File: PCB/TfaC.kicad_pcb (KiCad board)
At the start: 2 copper layers, 0 parts

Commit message: Added the switch footprints and started the layout
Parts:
- added ALMint1: ALMint, Pin_Headers:Pin_Header_Straight_1x01, F.Cu at (108.5, 116.3)
- added C201: 1u, Capacitors_SMD:C_0805_HandSoldering, F.Cu at (133.2, 98.9)
- added C202: 1u, Capacitors_SMD:C_0805_HandSoldering, F.Cu at (182.6, 78.1)
- added C203: 1u, Capacitors_SMD:C_0805_HandSoldering, F.Cu at (177.7, 82.8)
- added C204: 1u, Capacitors_SMD:C_0805_HandSoldering, F.Cu at (129.7, 94.8)
- added C501: 100n, Capacitors_SMD:C_0805_HandSoldering, F.Cu at (150.1, 95.1)
- added DCFint1: DCFint, Pin_Headers:Pin_Header_Straight_1x01, F.Cu at (112.0, 116.3)
- added IC501: ATMEGA88-A, Housings_QFP:LQFP-32_7x7mm_Pitch0.8mm, F.Cu at (147.3, 88.8)
- added M301: DisplayModule, Pin_Headers:Pin_Header_Angled_1x05, F.Cu at (167.0, 114.0)
- added P101: Line, Pin_Headers:Pin_Header_Straight_1x02, F.Cu at (193.2, 67.9)
- added P201: GND, Pin_Headers:Pin_Header_Straight_1x01, F.Cu at (183.5, 68.1)
- added P202: Vin, Pin_Headers:Pin_Header_Straight_1x01, F.Cu at (180.0, 68.1)
- added P203: Vcc, Pin_Headers:Pin_Header_Straight_1x01, F.Cu at (193.7, 73.9)
- added P204: Vbb, Pin_Headers:Pin_Header_Straight_1x01, F.Cu at (199.0, 86.2)
- added P501: PRG, Pin_Headers:Pin_Header_Straight_2x03, F.Cu at (139.8, 75.4)
- added Q401: IRLML2502, tfac-footprints:Micro3, F.Cu at (121.7, 104.1)
- added Q402: IRLML2502, tfac-footprints:Micro3, F.Cu at (114.2, 104.1)
- added Q403: IRLML2502, tfac-footprints:Micro3, F.Cu at (124.1, 87.9)
- added Q404: IRLML2502, tfac-footprints:Micro3, F.Cu at (109.3, 87.9)
- added Q405: IRLML2502, tfac-footprints:Micro3, F.Cu at (101.9, 87.9)
- added Q406: IRLML2502, tfac-footprints:Micro3, F.Cu at (116.7, 87.9)
- added Q407: NOPOP, tfac-footprints:Micro3, F.Cu at (106.8, 104.1)
- added Q408: IRLML2502, tfac-footprints:Micro3, F.Cu at (99.3, 104.3)
- added R201: 0, Resistors_SMD:R_0805_HandSoldering, F.Cu at (135.6, 99.0)
- added R401: 10K, Resistors_SMD:R_0805_HandSoldering, F.Cu at (124.7, 104.9)
- added R402: 1K5, Resistors_SMD:R_0805_HandSoldering, F.Cu at (122.4, 101.2)
- added R403: 10K, Resistors_SMD:R_0805_HandSoldering, F.Cu at (117.2, 104.9)
- added R404: 1K5, Resistors_SMD:R_0805_HandSoldering, F.Cu at (114.9, 101.2)
- added R405: 10K, Resistors_SMD:R_0805_HandSoldering, F.Cu at (121.2, 87.1)
- added R406: 4K7, Resistors_SMD:R_0805_HandSoldering, F.Cu at (123.3, 90.8)
- added R407: 10K, Resistors_SMD:R_0805_HandSoldering, F.Cu at (106.4, 87.1)
- added R408: 4K7, Resistors_SMD:R_0805_HandSoldering, F.Cu at (108.6, 90.8)
- added R409: 10K, Resistors_SMD:R_0805_HandSoldering, F.Cu at (98.8, 87.1)
- added R410: 4K7, Resistors_SMD:R_0805_HandSoldering, F.Cu at (101.1, 90.8)
- added R411: 10K, Resistors_SMD:R_0805_HandSoldering, F.Cu at (113.8, 87.1)
- added R412: 4K7, Resistors_SMD:R_0805_HandSoldering, F.Cu at (116.0, 90.8)
- added R413: NOPOP, Resistors_SMD:R_0805_HandSoldering, F.Cu at (109.9, 105.0)
- added R414: NOPOP, Resistors_SMD:R_0805_HandSoldering, F.Cu at (107.6, 101.2)
- added R415: 10K, Resistors_SMD:R_0805_HandSoldering, F.Cu at (102.4, 105.0)
- added R416: 4K7, Resistors_SMD:R_0805_HandSoldering, F.Cu at (100.1, 101.3)
- added R501: 10K, Resistors_SMD:R_0805_HandSoldering, F.Cu at (150.2, 97.4)
- added SW501: Time Set, tfac-footprints:TL3315, B.Cu at (171.5, 80.5)
- added SW502: Alarm Set, tfac-footprints:TL3315, B.Cu at (186.0, 80.5)
- added SW503: Fast, tfac-footprints:TL3315, B.Cu at (171.5, 95.5)
- added SW504: Slow, tfac-footprints:TL3315, B.Cu at (186.0, 95.5)
- added SW505: Auto Time, tfac-footprints:AYZ0202AGRLC, B.Cu at (161.5, 74.0)
- added SW506: Sleep, tfac-footprints:TL3315, F.Cu at (198.0, 115.5)
- added SW507: Summer Time, Pin_Headers:Pin_Header_Straight_1x02, F.Cu at (169.8, 68.3)
- added SW508: Alarm Enabled, tfac-footprints:CLSB12C01, F.Cu at (161.2, 86.2)
- added TP-MISO1: MISO, Pin_Headers:Pin_Header_Straight_1x01, F.Cu at (105.4, 75.4)
- added TP-MOSI1: MOSI, Pin_Headers:Pin_Header_Straight_1x01, F.Cu at (109.2, 75.4)
- added TP-Pint1: Pint, Pin_Headers:Pin_Header_Straight_1x01, F.Cu at (115.6, 116.3)
- added TP-SCK1: SCK, Pin_Headers:Pin_Header_Straight_1x01, F.Cu at (113.0, 75.6)
- added TP-SS1: SS1, Pin_Headers:Pin_Header_Straight_1x01, F.Cu at (156.5, 109.3)
- added TP-SS2: SS2, Pin_Headers:Pin_Header_Straight_1x01, F.Cu at (116.7, 75.6)
- added U201: MCP1703T-5002E/CB, tfac-footprints:SOT-23A, F.Cu at (199.0, 72.4)
- added U202: LD2979, tfac-footprints:SOT-23-5L, F.Cu at (129.6, 97.7)
- added U401: RTC-DCF77, tfac-footprints:RTC-DCF, F.Cu at (111.8, 96.2)
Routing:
- net L_MISO: track 0.00 -> 15.3 mm
- net ~L_SS: track 0.00 -> 11.9 mm
- net L_MOSI: track 0.00 -> 9.52 mm
- net L_SCK: track 0.00 -> 8.09 mm
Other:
- net class Default: clearance 0.2 -> 0.254; trace_width 0.25 -> 0.254; via_dia 0.6 -> 0.6858; via_drill 0.4 -> 0.3302
- rule trace_clearance: 0.2 -> 0.254
- rule trace_min: 0.2 -> 0.1524
- rule via_min_drill: 0.3 -> 0.3302
- rule via_min_size: 0.4 -> 0.6858

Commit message: Started the layout
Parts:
- removed ALMint1: ALMint, Pin_Headers:Pin_Header_Straight_1x01
- removed DCFint1: DCFint, Pin_Headers:Pin_Header_Straight_1x01
- removed P201: GND, Pin_Headers:Pin_Header_Straight_1x01
- removed P202: Vin, Pin_Headers:Pin_Header_Straight_1x01
- removed P203: Vcc, Pin_Headers:Pin_Header_Straight_1x01
- removed P204: Vbb, Pin_Headers:Pin_Header_Straight_1x01
- removed TP-MISO1: MISO, Pin_Headers:Pin_Header_Straight_1x01
- removed TP-MOSI1: MOSI, Pin_Headers:Pin_Header_Straight_1x01
- removed TP-Pint1: Pint, Pin_Headers:Pin_Header_Straight_1x01
- removed TP-SCK1: SCK, Pin_Headers:Pin_Header_Straight_1x01
- added REF**: MountingHole_2-7mm, Mounting_Holes:MountingHole_2-7mm, F.Cu at (103.0, 76.0)
- added REF**: MountingHole_2-7mm, Mounting_Holes:MountingHole_2-7mm, F.Cu at (142.0, 76.0)
- added REF**: MountingHole_2-7mm, Mounting_Holes:MountingHole_2-7mm, F.Cu at (103.0, 86.0)
- added REF**: MountingHole_2-7mm, Mounting_Holes:MountingHole_2-7mm, F.Cu at (142.0, 86.0)
- added TP1: CONN_01X06, Pin_Headers:Pin_Header_Straight_1x06, F.Cu at (102.1, 96.3)
- added TP2: CONN_01X06, Pin_Headers:Pin_Header_Straight_1x06, F.Cu at (143.0, 96.3)
- M301: footprint Pin_Headers:Pin_Header_Angled_1x05 -> Pin_Headers:Pin_Header_Straight_1x05
- SW506: moved to B.Cu
- moved C201 62.1 mm to (189.0, 71.6)
- moved C204 59.3 mm to (182.6, 68.1)
- moved U202 59.2 mm to (182.6, 71.4)
- moved R201 57.8 mm to (186.4, 71.6)
- moved R416 56.4 mm to (155.7, 110.7), turned to 270 degrees
- moved Q408 52.2 mm to (151.1, 110.7), turned to 270 degrees
- moved P501 48.8 mm to (178.3, 105.4), turned to 90 degrees
- moved R414 48.0 mm to (155.4, 104.1), turned to 270 degrees
- moved R415 45.6 mm to (147.6, 110.7)
- moved Q407 44.3 mm to (151.1, 104.1), turned to 270 degrees
- moved R404 40.6 mm to (155.4, 98.0), turned to 270 degrees
- moved C501 38.7 mm to (188.0, 87.1), turned to 90 degrees
- moved R413 37.7 mm to (147.6, 104.4)
- moved Q402 37.2 mm to (150.9, 98.0), turned to 270 degrees
- moved R501 36.7 mm to (185.4, 87.1), turned to 270 degrees
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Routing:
- net /Controller/SCK: track 0.19 -> 126.4 mm, vias 0 -> 2
- net /Controller/MISO: track 0.19 -> 111.3 mm
- net /Power System/Vbb: track 0.00 -> 96.5 mm, vias 0 -> 7
- net GND: track 0.00 -> 73.4 mm, vias 0 -> 6
- net /Controller/~DISPLAY_SELECT: track 0.00 -> 52.9 mm, vias 0 -> 1
- net /Controller/MOSI: track 0.19 -> 34.7 mm
- net /Power System/Vin: track 0.00 -> 24.0 mm
- net Fast: track 0.00 -> 18.3 mm, vias 0 -> 1
- net Alarm_Enabled: track 0.00 -> 16.8 mm
- net L_ALARM_INT: track 0.00 -> 16.7 mm
- net L_Periodic_INT: track 0.00 -> 16.5 mm
- net Reset: track 0.00 -> 16.5 mm, vias 0 -> 4
- net L_Rx: track 0.00 -> 13.9 mm
- net Slow: track 0.00 -> 13.8 mm, vias 0 -> 1
- net L_DCF_RCPT: track 0.00 -> 13.3 mm
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- added copper zone on B.Cu, net /Power System/Vbb
- added copper zone on F.Cu, net GND
- added copper zone on B.Cu, net Reset

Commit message: Trying out an alternative layout
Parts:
- moved P101 50.3 mm to (147.6, 68.1)
- moved C202 48.0 mm to (149.6, 79.5), turned to 270 degrees
- moved U201 44.3 mm to (153.2, 79.5), turned to 270 degrees
- moved R201 42.6 mm to (146.3, 85.9)
- moved REF** 42.5 mm to (99.5, 74.8), turned to 90 degrees
- moved C204 41.4 mm to (148.6, 91.7), turned to 180 degrees
- moved C203 40.2 mm to (153.2, 82.3), turned to 180 degrees
- moved C201 40.0 mm to (151.6, 85.9), turned to 270 degrees
- moved U202 37.6 mm to (149.1, 88.4), turned to 270 degrees
- moved REF** 36.6 mm to (99.5, 112.5), turned to 90 degrees
- moved REF** 34.4 mm to (109.5, 74.8), turned to 90 degrees
- moved R409 32.8 mm to (123.4, 83.4), turned to 90 degrees
- moved R416 31.9 mm to (140.0, 83.1)
- moved Q405 31.1 mm to (120.0, 83.2), turned to 90 degrees
- moved Q408 31.0 mm to (136.7, 83.3)
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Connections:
- C203 pad 1: Reset -> /Controller/Vcc
- C501 pad 1: Reset -> /Controller/Vcc
- IC501 pad 12: (no net) -> Net-(IC501-Pad12)
- IC501 pad 18: Net-(IC501-Pad18) -> /Controller/Vcc
- IC501 pad 19: (no net) -> Net-(IC501-Pad19)
- IC501 pad 20: (no net) -> Net-(IC501-Pad20)
- IC501 pad 22: (no net) -> Net-(IC501-Pad22)
- IC501 pad 26: (no net) -> Net-(IC501-Pad26)
- IC501 pad 27: (no net) -> Net-(IC501-Pad27)
- IC501 pad 28: (no net) -> Net-(IC501-Pad28)
- IC501 pad 4: Net-(IC501-Pad18) -> /Controller/Vcc
- IC501 pad 6: Net-(IC501-Pad18) -> /Controller/Vcc
- IC501 pad 7: (no net) -> Net-(IC501-Pad7)
- IC501 pad 8: (no net) -> Net-(IC501-Pad8)
- M301 pad 1: Reset -> /Controller/Vcc
- M301 pad 3: /Controller/MOSI -> /Controller/SCK
- M301 pad 4: /Controller/SCK -> /Controller/~DISPLAY_SELECT
- M301 pad 5: /Controller/~DISPLAY_SELECT -> GND
- P501 pad 2: Reset -> /Controller/Vcc
- R402 pad 1: Reset -> /Controller/Vcc
- R404 pad 1: Reset -> /Controller/Vcc
- R406 pad 1: Reset -> /Controller/Vcc
- R408 pad 1: Reset -> /Controller/Vcc
- R410 pad 1: Reset -> /Controller/Vcc
- R412 pad 1: Reset -> /Controller/Vcc
- R414 pad 1: Reset -> /Controller/Vcc
- R416 pad 1: Reset -> /Controller/Vcc
- R501 pad 1: Net-(IC501-Pad18) -> /Controller/Vcc
- SW505 pad 1: (no net) -> Net-(SW505-Pad1)
- SW508 pad 1: (no net) -> Net-(SW508-Pad1)
- U201 pad 3: Reset -> /Controller/Vcc
- U202 pad 4: (no net) -> Net-(U202-Pad4)
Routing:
- net /Controller/SCK: track 126.4 -> 11.6 mm, vias 2 -> 0
- net /Controller/MISO: track 111.3 -> 11.5 mm
- net /Controller/Vcc: track 0.00 -> 57.4 mm, vias 0 -> 5
- net /Power System/Vbb: track 96.5 -> 43.6 mm, vias 7 -> 8
- net /Controller/~DISPLAY_SELECT: track 52.9 -> 8.05 mm, vias 1 -> 0
- net GND: track 73.4 -> 36.0 mm, vias 6 -> 7
- net /Controller/MOSI: track 34.7 -> 10.9 mm
- net L_MISO: track 15.3 -> 38.5 mm
- net L_Periodic_INT: track 16.5 -> 38.8 mm
- net L_MOSI: track 10.8 -> 30.4 mm
- net L_DCF_RCPT: track 13.3 -> 30.8 mm
- net L_SCK: track 8.87 -> 21.9 mm
- net /Power System/Vin: track 24.0 -> 11.7 mm, vias 0 -> 3
- net Reset: track 16.5 -> 4.39 mm, vias 4 -> 0
- net /Controller/~RTC_SELECT: track 9.87 -> 21.9 mm
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- added copper zone on B.Cu, net /Controller/Vcc
- added copper zone on B.Cu, net /Power System/Vin
- removed copper zone on B.Cu, net Reset
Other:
- net class Default: clearance 0.254 -> 0.1524; trace_width 0.254 -> 0.1524
- rule trace_clearance: 0.254 -> 0.1524

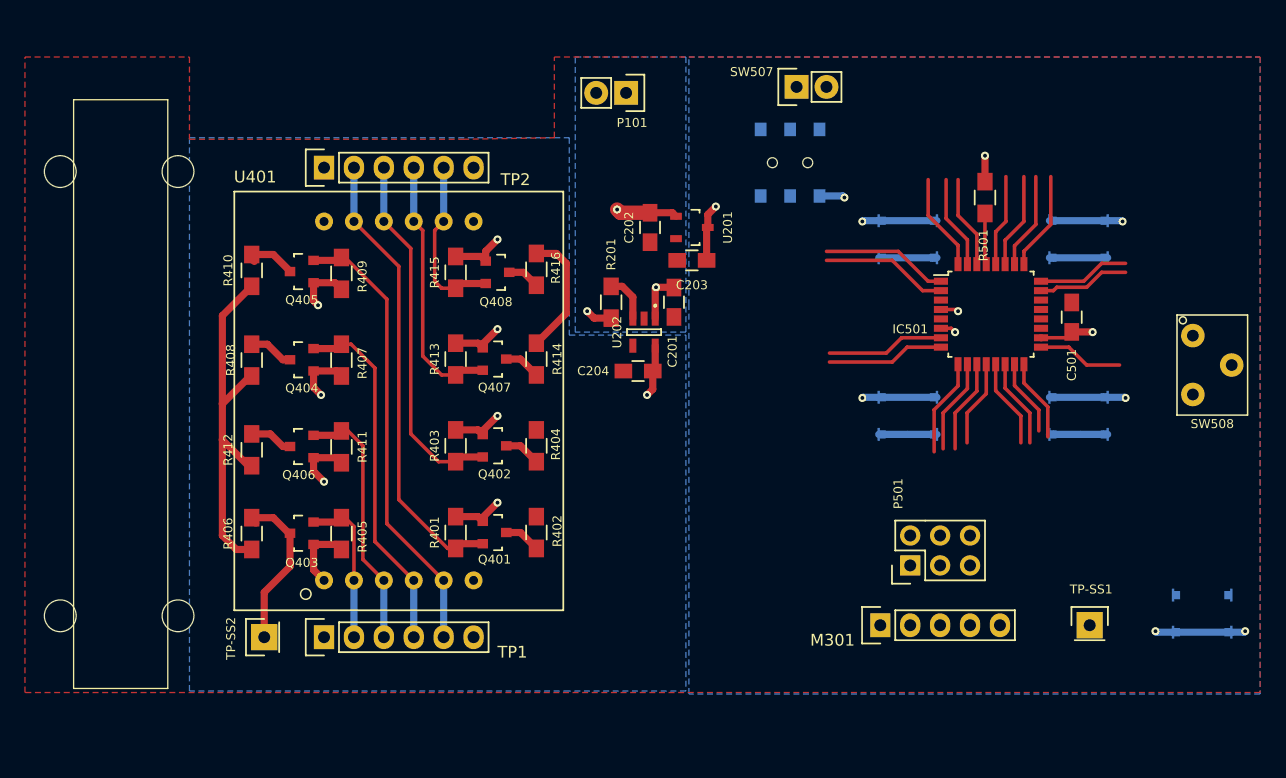
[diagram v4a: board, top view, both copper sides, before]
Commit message: Completed draft layout for the alternate layout
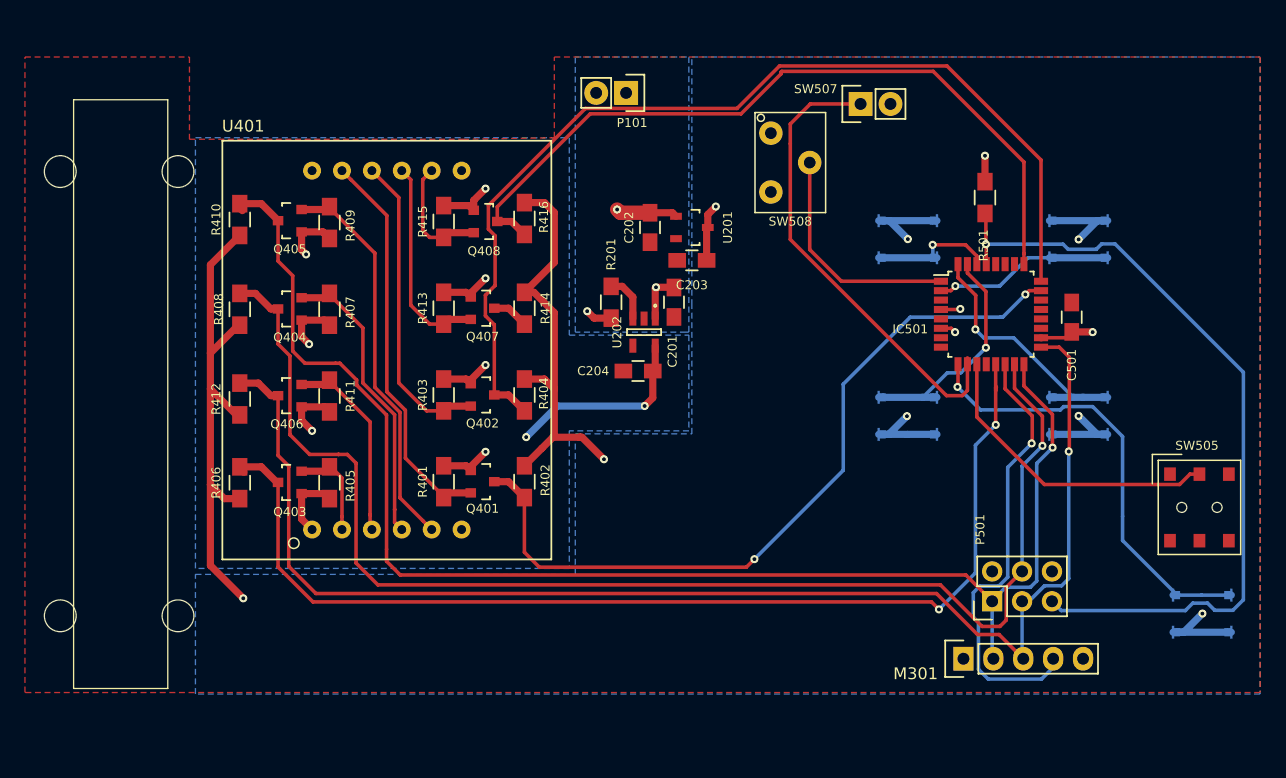
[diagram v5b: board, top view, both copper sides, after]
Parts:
- removed TP-SS1: SS1, Pin_Headers:Pin_Header_Straight_1x01
- removed TP-SS2: SS2, Pin_Headers:Pin_Header_Straight_1x01
- removed TP1, TP2: CONN_01X06, Pin_Headers:Pin_Header_Straight_1x06
- SW505: moved to F.Cu
- moved SW505 45.5 mm to (196.3, 103.3)
- moved SW508 39.8 mm to (161.5, 74.0)
- moved M301 7.61 mm to (176.2, 116.1)
- moved P501 7.60 mm to (178.7, 111.3)
- moved SW507 5.63 mm to (167.5, 69.0)
- moved R416 4.44 mm to (138.9, 78.7)
- moved Q406 4.44 mm to (119.0, 93.8)
- moved R402 4.44 mm to (138.9, 101.1)
- moved R404 4.44 mm to (138.9, 93.7)
- moved R414 4.44 mm to (138.9, 86.4)
- moved Q403 4.44 mm to (119.0, 101.2)
- moved R405 4.44 mm to (122.4, 101.2)
- moved R406 4.44 mm to (114.8, 101.2)
- moved R407 4.44 mm to (122.4, 86.4)
- moved R408 4.44 mm to (114.8, 86.4)
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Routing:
- net /Controller/MISO: track 11.5 -> 121.3 mm, vias 0 -> 1
- net /Controller/SCK: track 11.6 -> 116.1 mm, vias 0 -> 1
- net /Controller/MOSI: track 10.9 -> 112.4 mm, vias 0 -> 1
- net /Controller/DCF_RCPT: track 10.9 -> 85.5 mm
- net /Controller/~RTC_SELECT: track 21.9 -> 92.6 mm, vias 0 -> 2
- net Reset: track 4.39 -> 68.1 mm, vias 0 -> 1
- net /Controller/Periodic_INT: track 10.9 -> 66.2 mm, vias 0 -> 2
- net /Controller/ALARM_INT: track 11.1 -> 65.5 mm
- net /Controller/Vcc: track 57.4 -> 93.7 mm, vias 5 -> 7
- net Summer_Time: track 8.03 -> 40.0 mm
- net /Controller/~DISPLAY_SELECT: track 8.05 -> 38.5 mm, vias 0 -> 1
- net Sleep: track 8.27 -> 38.4 mm, vias 0 -> 1
- net Auto_Time: track 7.95 -> 26.1 mm
- net /Power System/Vbb: track 43.6 -> 56.1 mm, vias 8 -> 9
- net Net-(IC501-Pad7): track 10.0 -> 0.00 mm
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
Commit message: Completed the layout and generated the Gerbers
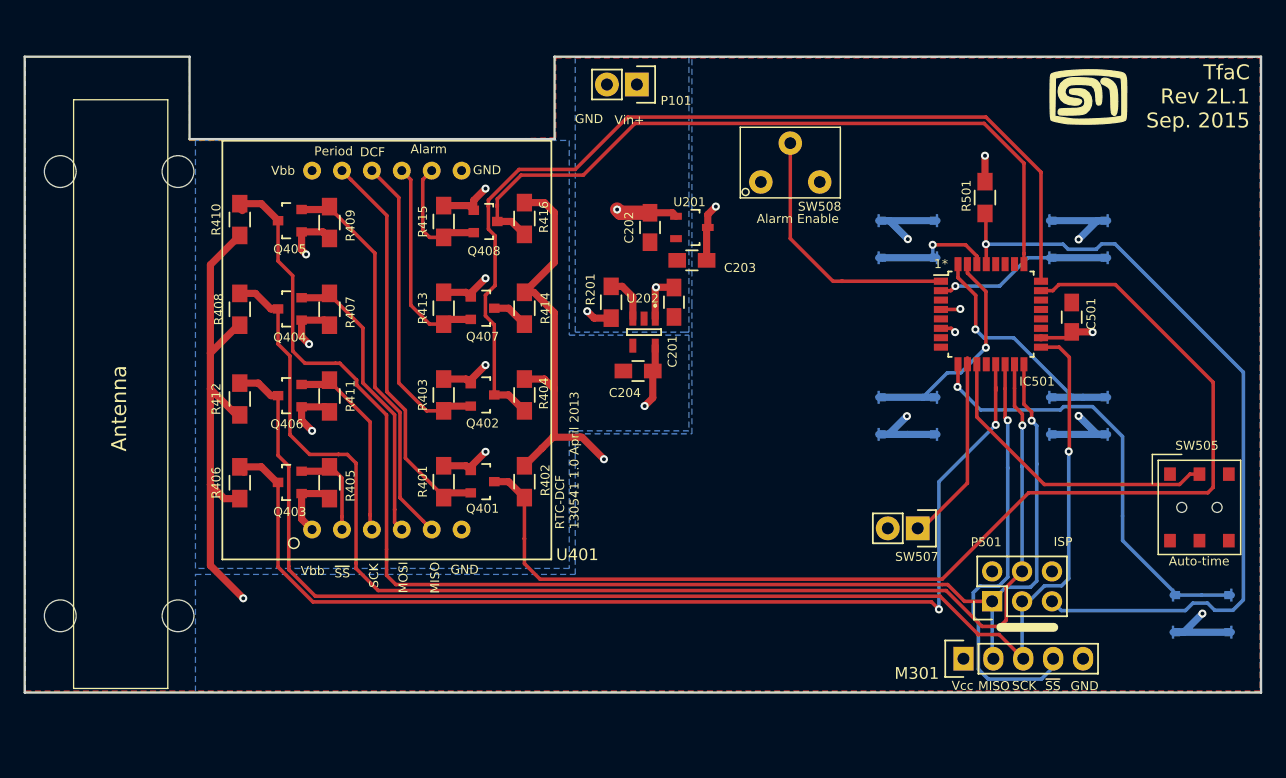
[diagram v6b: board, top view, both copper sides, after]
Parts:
- added G***: LOGO, tfac-footprints:myLogo_basic_rounded_50, F.Cu at (186.8, 68.4)
- moved SW507 36.4 mm to (172.3, 105.1), turned to 270 degrees
- moved P101 1.16 mm to (148.5, 67.4)
- turned SW508 to 0 degrees
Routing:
- net /Controller/Periodic_INT: track 66.2 -> 98.2 mm, vias 2 -> 0
- net Summer_Time: track 40.0 -> 16.5 mm
- net /Power System/Vbb: track 56.1 -> 45.0 mm, vias 9 -> 8
- net /Controller/DCF_RCPT: track 85.5 -> 81.7 mm
- net /Controller/ALARM_INT: track 65.5 -> 62.1 mm
- net Alarm_Enabled: track 19.6 -> 22.5 mm
- net /Controller/~DISPLAY_SELECT: track 38.5 -> 36.8 mm
- net /Controller/MOSI: track 112.4 -> 111.2 mm
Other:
- board outline added: 105 x 54 mm
- board text added: "1*"
- board text added: "Alarm"
- board text added: "Alarm Enable"
- board text added: "Alarm set"
- board text added: "Antenna"
- board text added: "Auto-time"
- board text added: "DCF"
- board text added: "Fast"
- board text added: "GND"
- board text added: "ISP"
- board text added: "MISO"
- board text added: "MOSI"
- board text added: "Period"
- board text added: "RTC-DCF 130541 1.0 April 2013"
- board text added: "SCK"
- board text added: "Sleep"
- board text added: "Slow"
- board text added: "TfaC Rev 2L.1 Sep. 2015"
- board text added: "Time set"
- board text added: "Vbb"
- board text added: "Vcc"
- board text added: "Vin+"
- board text added: "~SS"
